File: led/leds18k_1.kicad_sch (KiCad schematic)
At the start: 32 parts, among them Q13 IPS70R1K4P7SAKMA1, Q2 IPS70R1K4P7SAKMA1, U1 LM397, U2 4N25, U5 4N25

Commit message: schematics with 5050 leds ready
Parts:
- removed D5: 1.5KE440A, Diode_THT:D_DO-15_P5.08mm_Vertical_KathodeUp, symbol Device:D_Zener
- removed D6, D7, D8, D9: 1N5408, Diode_THT:D_DO-41_SOD81_P10.16mm_Horizontal, symbol Diode:1N4007
- removed ESMR401VSN102MA50S_3: ESMR401VSN102MA50S, arduino-library:CAPPRD1000W180D3550H5250, symbol Device:C_Polarized
- removed L1: HCTI-220-5.8, arduino-library:HCTI22058, symbol Device:L
- removed LED1, LED10, LED11, LED12, LED13, LED14, LED2, LED3, LED4, LED5, LED6, LED7, LED8, LED9: L150-18705024000H0, arduino-library:L15065705024000H0, symbol L150-65705024000H0:L150-65705024000H0
- removed Q13, Q2: IPS70R1K4P7SAKMA1, arduino-library:TO229P240X654X875-3P, symbol IPS70R1K4P7SAKMA1:IPS70R1K4P7SAKMA1
- removed R1: RSF1JT1R00, arduino-library:RESAD2900W85L1100D450, symbol RSF1JT1R00:RSF1JT1R00
- removed R4, R5, R6: MFR-25FTE52-100K, Resistor_THT:R_Axial_DIN0204_L3.6mm_D1.6mm_P2.54mm_Vertical, symbol Device:R
- removed RH2: MFR50SFTE52-1K, Resistor_THT:R_Axial_DIN0204_L3.6mm_D1.6mm_P2.54mm_Vertical, symbol Device:R
- removed TH1: CL60, Resistor_THT:R_Axial_DIN0516_L15.5mm_D5.0mm_P7.62mm_Vertical, symbol Device:Thermistor_NTC
- removed U1: LM397, Package_TO_SOT_SMD:SOT-23-5, symbol Comparator:LM397
- removed U2, U5: 4N25, Package_DIP:DIP-6_W7.62mm, symbol Isolator:4N25
- added D31, D32, D33, D34: 1N5408, Diode_THT:D_DO-41_SOD81_P10.16mm_Horizontal, symbol Diode:1N4007
- added D35: 1.5KE440A, Diode_THT:D_DO-15_P5.08mm_Vertical_KathodeUp, symbol Device:D_Zener
- added ESMR401VSN102MA50S_7: ESMR401VSN102MA50S, arduino-library:CAPPRD1000W180D3550H5250, symbol Device:C_Polarized
- added L7: HCTI-220-5.8, arduino-library:HCTI22058, symbol Device:L
- added LED85, LED86, LED87, LED88, LED89, LED90, LED91, LED92, LED93, LED94, LED95, LED96, LED97, LED98: L150-18705024000H0, arduino-library:L15065705024000H0, symbol L150-65705024000H0:L150-65705024000H0
- added Q19, Q20: IPS70R1K4P7SAKMA1, arduino-library:TO229P240X654X875-3P, symbol IPS70R1K4P7SAKMA1:IPS70R1K4P7SAKMA1
- added R34: RSF1JT1R00, arduino-library:RESAD2900W85L1100D450, symbol RSF1JT1R00:RSF1JT1R00
- added R35, R36, R37: MFR-25FTE52-100K, Resistor_THT:R_Axial_DIN0204_L3.6mm_D1.6mm_P2.54mm_Vertical, symbol Device:R
- added RH7: MFR50SFTE52-1K, Resistor_THT:R_Axial_DIN0204_L3.6mm_D1.6mm_P2.54mm_Vertical, symbol Device:R
- added TH7: CL60, Resistor_THT:R_Axial_DIN0516_L15.5mm_D5.0mm_P7.62mm_Vertical, symbol Device:Thermistor_NTC
- added U20, U22: 4N25, Package_DIP:DIP-6_W7.62mm, symbol Isolator:4N25
- added U21: LM397, Package_TO_SOT_SMD:SOT-23-5, symbol Comparator:LM397
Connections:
- net CURRENT_DRIVER_PWM: now also RH7.2, U21.1 (-)
- net GND: now also D32.1 (K), D34.1 (K), ESMR401VSN102MA50S_7.2, R34.1, U20.2, U20.4, U21.2 (V-), U22.2, U22.4
- net LEDS_ON: now also U20.1
- net MAINS_LIVE: now also D33.1 (K), D34.2 (A)
- net MAINS_ZERO: now also D31.1 (K), D32.2 (A)
- net VDD: now also R36.1, R37.1, U20.6, U21.5 (V+)
- new net: LED85.1 (K_1), LED85.2 (A_1)
- new net: LED85.3 (K_2), LED86.4 (A_2)
- new net: LED85.4 (A_2), LED98.3 (K_2)
- new net: LED92.1 (K_1), LED92.2 (A_1)
- new net: LED92.3 (K_2), LED93.4 (A_2)
- new net: D35.1 (K), ESMR401VSN102MA50S_7.1, LED92.4 (A_2), TH7.2
- new net: Q19.3 (S), R34.2, U21.3 (+)
- new net: LED96.1 (K_1), LED96.2 (A_1)
- new net: LED96.3 (K_2), LED97.4 (A_2)
- new net: LED95.3 (K_2), LED96.4 (A_2)
- new net: R36.2, RH7.1, U21.4, U22.1
- new net: LED93.1 (K_1), LED93.2 (A_1)
- new net: LED93.3 (K_2), LED94.4 (A_2)
- new net: Q20.1 (G), R35.1, U22.5
- new net: L7.1, LED91.3 (K_2), Q20.2 (D), R35.2
- new net: Q19.2 (D), Q20.3 (S)
- new net: Q19.1 (G), U20.5
- new net: D31.2 (A), D33.2 (A), TH7.1
- new net: LED94.1 (K_1), LED94.2 (A_1)
- new net: LED94.3 (K_2), LED95.4 (A_2)
- new net: LED98.1 (K_1), LED98.2 (A_1)
- new net: LED97.3 (K_2), LED98.4 (A_2)
- new net: LED87.1 (K_1), LED87.2 (A_1)
- new net: LED87.3 (K_2), LED88.4 (A_2)
- new net: LED86.3 (K_2), LED87.4 (A_2)
- new net: LED88.1 (K_1), LED88.2 (A_1)
- new net: LED88.3 (K_2), LED89.4 (A_2)
- new net: LED86.1 (K_1), LED86.2 (A_1)
- new net: R37.2, U22.6
- new net: LED90.1 (K_1), LED90.2 (A_1)
- new net: LED90.3 (K_2), LED91.4 (A_2)
- new net: LED89.3 (K_2), LED90.4 (A_2)
- new net: LED89.1 (K_1), LED89.2 (A_1)
- new net: LED91.1 (K_1), LED91.2 (A_1)
- new net: D35.2 (A), L7.2
- new net: LED97.1 (K_1), LED97.2 (A_1)
- new net: LED95.1 (K_1), LED95.2 (A_1)

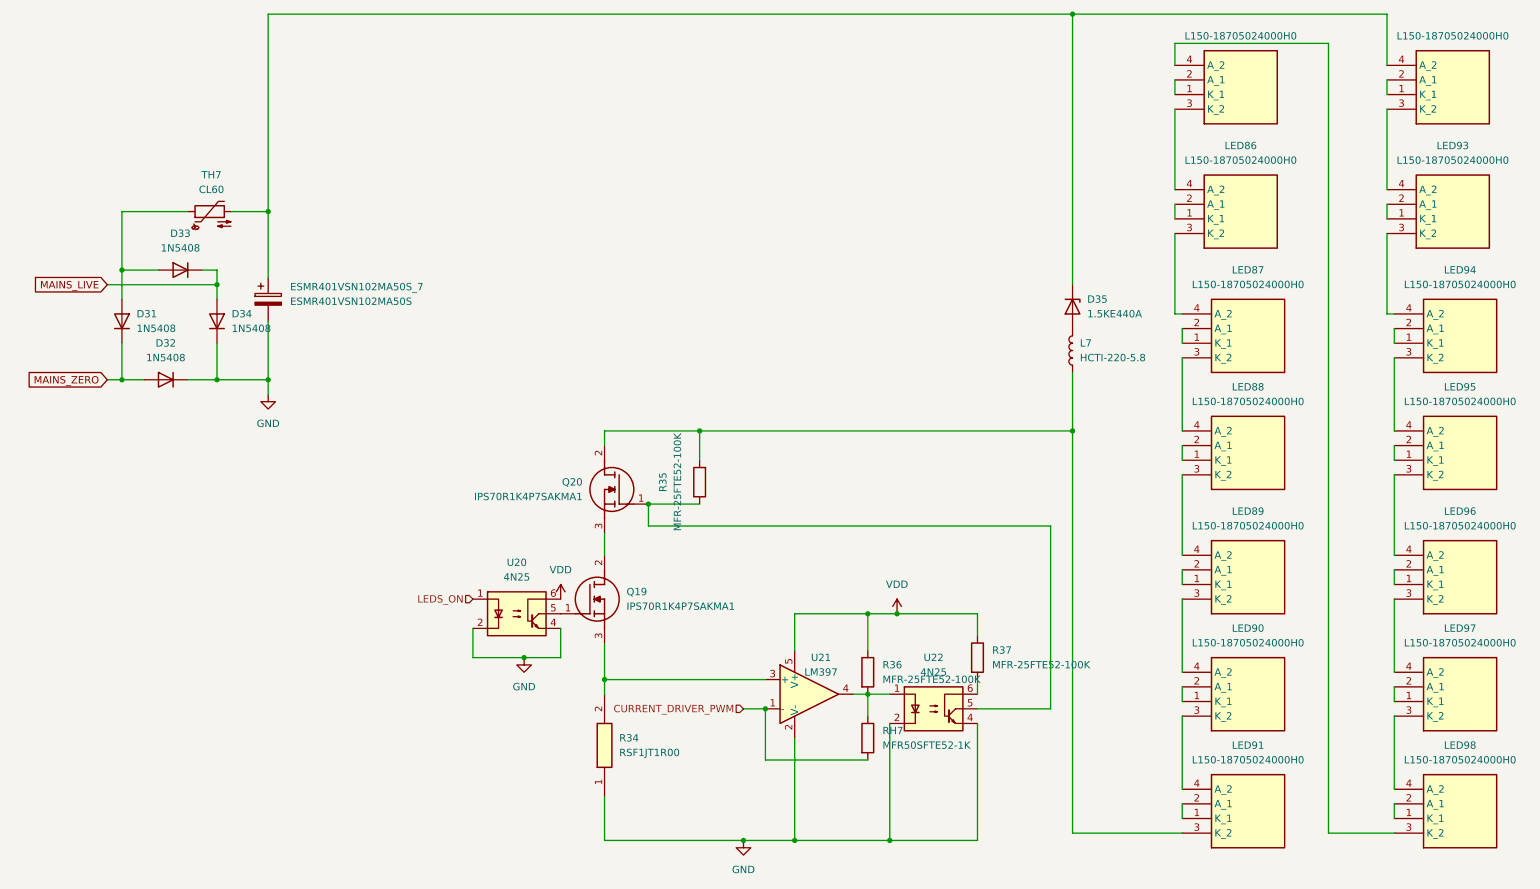
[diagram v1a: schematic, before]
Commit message: using single and dual top switch current driver circuits
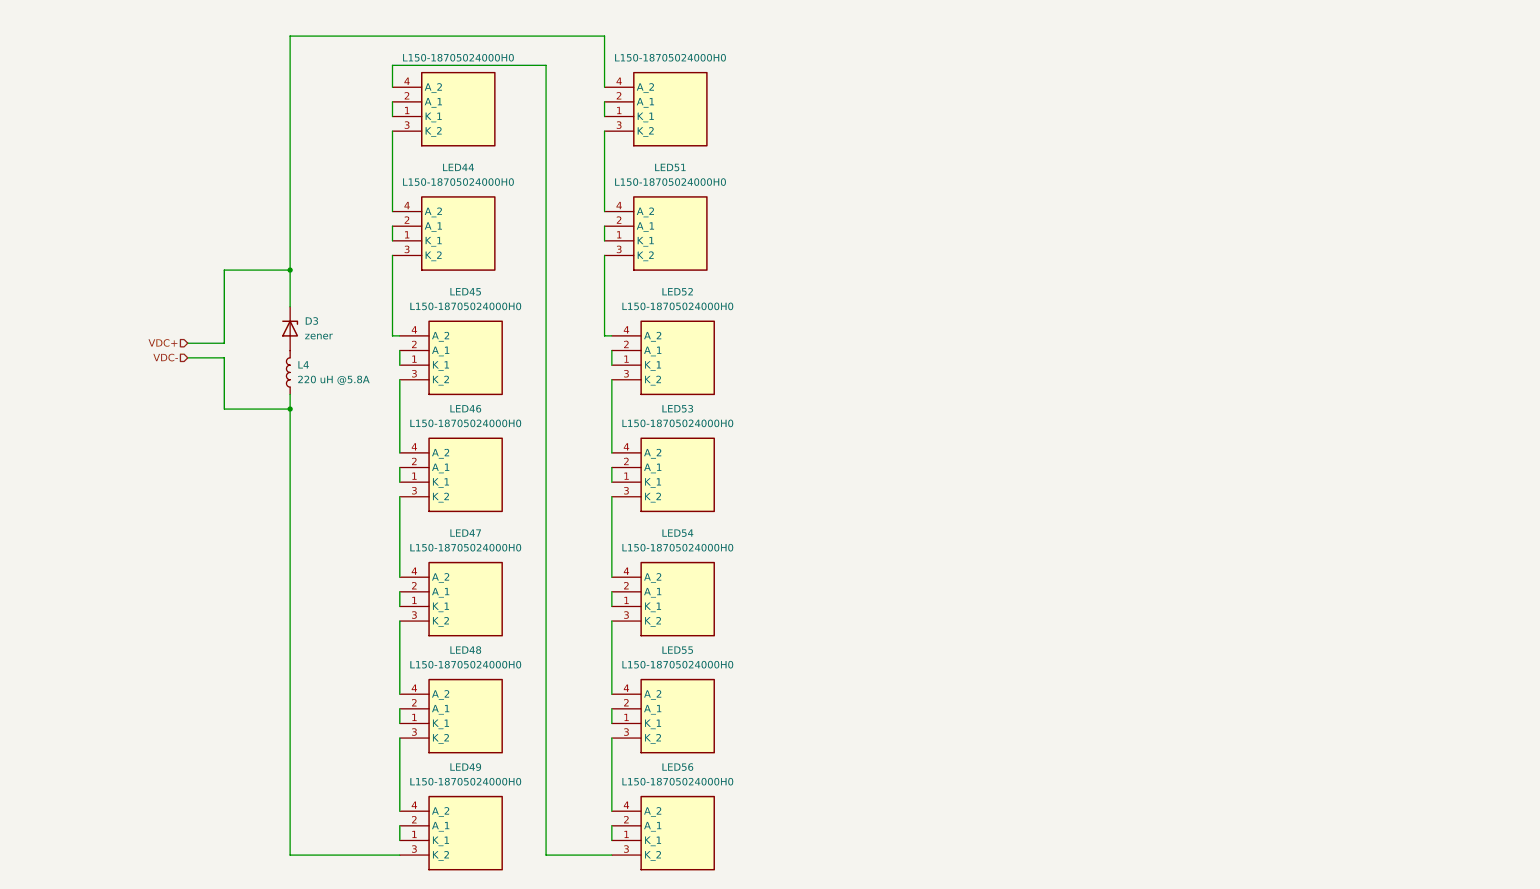
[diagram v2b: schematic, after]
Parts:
- removed D31, D32, D33, D34: 1N5408, Diode_THT:D_DO-41_SOD81_P10.16mm_Horizontal, symbol Diode:1N4007
- removed ESMR401VSN102MA50S_7: ESMR401VSN102MA50S, arduino-library:CAPPRD1000W180D3550H5250, symbol Device:C_Polarized
- removed Q19, Q20: IPS70R1K4P7SAKMA1, arduino-library:TO229P240X654X875-3P, symbol IPS70R1K4P7SAKMA1:IPS70R1K4P7SAKMA1
- removed R34: RSF1JT1R00, arduino-library:RESAD2900W85L1100D450, symbol RSF1JT1R00:RSF1JT1R00
- removed R35, R36, R37: MFR-25FTE52-100K, Resistor_THT:R_Axial_DIN0204_L3.6mm_D1.6mm_P2.54mm_Vertical, symbol Device:R
- removed RH7: MFR50SFTE52-1K, Resistor_THT:R_Axial_DIN0204_L3.6mm_D1.6mm_P2.54mm_Vertical, symbol Device:R
- removed TH7: CL60, Resistor_THT:R_Axial_DIN0516_L15.5mm_D5.0mm_P7.62mm_Vertical, symbol Device:Thermistor_NTC
- removed U20, U22: 4N25, Package_DIP:DIP-6_W7.62mm, symbol Isolator:4N25
- removed U21: LM397, Package_TO_SOT_SMD:SOT-23-5, symbol Comparator:LM397
- D3: renamed from D35; value 1.5KE440A -> zener; Mouser Part Number (none) -> 603-1.5KE440A/B
- L4: renamed from L7; value HCTI-220-5.8 -> 220 uH @5.8A; Mouser Part Number (none) -> 530-HCTI-220-5.8
- LED43: renamed from LED85; Mouser Part Number 997-L150657050240H0 -> 997-L15018705024000H
- LED44: renamed from LED86; Mouser Part Number 997-L150657050240H0 -> 997-L15018705024000H
- LED45: renamed from LED87; Mouser Part Number 997-L150657050240H0 -> 997-L15018705024000H
- LED46: renamed from LED88; Mouser Part Number 997-L150657050240H0 -> 997-L15018705024000H
- LED47: renamed from LED89; Mouser Part Number 997-L150657050240H0 -> 997-L15018705024000H
- LED48: renamed from LED90; Mouser Part Number 997-L150657050240H0 -> 997-L15018705024000H
- LED49: renamed from LED91; Mouser Part Number 997-L150657050240H0 -> 997-L15018705024000H
- LED50: renamed from LED92; Mouser Part Number 997-L150657050240H0 -> 997-L15018705024000H
- LED51: renamed from LED93; Mouser Part Number 997-L150657050240H0 -> 997-L15018705024000H
- LED52: renamed from LED94; Mouser Part Number 997-L150657050240H0 -> 997-L15018705024000H
- LED53: renamed from LED95; Mouser Part Number 997-L150657050240H0 -> 997-L15018705024000H
- LED54: renamed from LED96; Mouser Part Number 997-L150657050240H0 -> 997-L15018705024000H
- LED55: renamed from LED97; Mouser Part Number 997-L150657050240H0 -> 997-L15018705024000H
- LED56: renamed from LED98; Mouser Part Number 997-L150657050240H0 -> 997-L15018705024000H
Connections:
- net VDC+: now reaches D3.1 (K), LED50.4 (A_2)
- net VDC-: now reaches L4.1, LED49.3 (K_2)
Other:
- moved on the sheet: D3, L4, LED44, LED45, LED46, LED47, LED48, LED49, LED51, LED52, LED53, LED54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

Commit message: led pcb designed
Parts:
- added H12, H16: MountingHole_Pad, Connector_Pin:Pin_D1.0mm_L10.0mm_LooseFit, symbol Mechanical:MountingHole_Pad
- D3: footprint Diode_THT:D_DO-15_P5.08mm_Vertical_KathodeUp -> arduino-library:DIOM7959X262N; Mouser Part Number 603-1.5KE440A/B -> 833-SMCJ1.5KE440A-TP
- L4: footprint arduino-library:HCTI22058 -> arduino-library:Coil_6cmx1cm
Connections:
- net VDC+: now also H12.1
- net VDC-: now also H16.1
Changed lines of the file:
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@@
 	(paper "A4")
+	(junction
+		(at 54.61 73.66)
+		(diameter 0)
+		(color 0 0 0 0)
+	)
 	(junction
 		(at 69.85 85.09)
@@
 	)
 	(junction
+		(at 54.61 76.2)
+		(diameter 0)
+		(color 0 0 0 0)
+	)
+	(junction
 		(at 69.85 60.96)
 		(diameter 0)
@@
 	(wire
 		(pts
-			(xy 52.07 73.66) (xy 58.42 73.66)
+			(xy 52.07 73.66) (xy 54.61 73.66)
 		)
 		(stroke
@@
 	(wire
 		(pts
+			(xy 54.61 73.66) (xy 58.42 73.66)
+		)
+		(stroke
+			(width 0)
+			(type default)
+		)
+	)
+	(wire
+		(pts
 			(xy 69.85 20.32) (xy 69.85 60.96)
 		)
@@
 	(wire
 		(pts
-			(xy 52.07 76.2) (xy 58.42 76.2)
+			(xy 52.07 76.2) (xy 54.61 76.2)
 		)
 		(stroke
@@
 		(pts
 			(xy 88.9 121.92) (xy 88.9 134.62)
+		)
+		(stroke
+			(width 0)
+			(type default)
+		)
+	)
+	(wire
+		(pts
+			(xy 54.61 76.2) (xy 58.42 76.2)
 		)
 		(stroke
@@
 	)
 	(symbol
+		(lib_id "Mechanical:MountingHole_Pad")
+		(at 54.61 78.74 180)
+		(unit 1)
+		(exclude_from_sim no)
+		(in_bom no)
+		(on_board yes)
+		(dnp no)
+		(fields_autoplaced yes)
+		(property "Reference" "H16"
+			(at 57.15 78.7399 0)
+			(effects
+				(font
+					(size 1.27 1.27)
+				)
+				(justify right)
+			)
+		)
+		(property "Value" "MountingHole_Pad"
+			(at 57.15 81.2799 0)
+			(effects
+				(font
+					(size 1.27 1.27)
+				)
+				(justify right)
+			)
+		)
+		(property "Footprint" "Connector_Pin:Pin_D1.0mm_L10.0mm_LooseFit"
+			(at 54.61 78.74 0)
+			(effects
+				(font
+					(size 1.27 1.27)
+				)
+				(hide yes)
+			)
+		)
+		(property "Datasheet" "~"
+			(at 54.61 78.74 0)
+			(effects
+				(font
+					(size 1.27 1.27)
+				)
+				(hide yes)
+			)
+		)
+		(property "Description" "Mounting Hole with connection"
+			(at 54.61 78.74 0)
+			(effects
+				(font
+					(size 1.27 1.27)
+				)
+				(hide yes)
+			)
+		)
+		(pin "1"
+		)
+		(instances
+			(project "led"
+				(path "/3f432d6c-3758-4345-b186-9310705dc61b/4657a6da-42a0-4c37-9dff-046ab29fe1ba"
+					(reference "H16")
+					(unit 1)
+				)
+				(path "/3f432d6c-3758-4345-b186-9310705dc61b/5aec1ce1-45e4-46e9-8146-4644b64be076"
+					(reference "H17")
+					(unit 1)
+				)
+				(path "/3f432d6c-3758-4345-b186-9310705dc61b/a148affd-8e36-468c-8c01-ab2086054996"
+					(reference "H18")
+					(unit 1)
+				)
+				(path "/3f432d6c-3758-4345-b186-9310705dc61b/e5c4d2d5-aef7-4d79-b2d9-7e80d0bdca31"
+					(reference "H19")
+					(unit 1)
+				)
+			)
+		)
+	)
+	(symbol
 		(lib_id "L150-65705024000H0:L150-65705024000H0")
 		(at 88.9 80.01 0)
@@
 			)
 		)
-		(property "Footprint" "arduino-library:HCTI22058"
+		(property "Footprint" "arduino-library:Coil_6cmx1cm"
 			(at 69.85 78.74 0)
 			(effects
@@
 			)
 		)
-		(property "Description" "Inductor"
+		(property "Description" "Inductor coil radius=1cm, length=5.5cm, turns=3*55=165, wire radius=1mm air or wood core"
 			(at 69.85 78.74 0)
 			(effects
@@
 			)
 		)
-		(property "Footprint" "Diode_THT:D_DO-15_P5.08mm_Vertical_KathodeUp"
+		(property "Footprint" "arduino-library:DIOM7959X262N"
 			(at 69.85 71.12 0)
 			(effects
@@
 			)
 		)
-		(property "Datasheet" "https://www.littelfuse.com/assetdocs/tvs-diodes-1-5ke-datasheet?assetguid=9D02C7D2-86A5-4BFF-9251-966D6AF02BF7"
+		(property "Datasheet" "https://hu.mouser.com/datasheet/3/225/1/SMCJ1.5KE6.8(C)A-SMCJ1.5KE550(C)A(DO-214AB).pdf"
 			(at 69.85 71.12 0)
 			(effects
@@
 			)
 		)
-		(property "Mouser Part Number" "603-1.5KE440A/B"
+		(property "Mouser Part Number" "833-SMCJ1.5KE440A-TP"
 			(at 69.85 71.12 90)
 			(effects
@@
 					(unit 1)
 				)
+			)
+		)
+	)
+	(symbol
+		(lib_id "Mechanical:MountingHole_Pad")
+		(at 54.61 71.12 0)
+		(unit 1)
+		(exclude_from_sim no)
+		(in_bom no)
+		(on_board yes)
+		(dnp no)
+		(fields_autoplaced yes)
+		(property "Reference" "H12"
+			(at 57.15 68.5799 0)
+			(effects
+				(font
+					(size 1.27 1.27)
+				)
+				(justify left)
+			)
+		)
+		(property "Value" "MountingHole_Pad"
+			(at 57.15 71.1199 0)
+			(effects
+				(font
+					(size 1.27 1.27)
+				)
+				(justify left)
+			)
+		)
+		(property "Footprint" "Connector_Pin:Pin_D1.0mm_L10.0mm_LooseFit"
+			(at 54.61 71.12 0)
+			(effects
+				(font
+					(size 1.27 1.27)
+				)
+				(hide yes)
+			)
+		)
+		(property "Datasheet" "~"
+			(at 54.61 71.12 0)
+			(effects
+				(font
+					(size 1.27 1.27)
+				)
+				(hide yes)
+			)
+		)
+		(property "Description" "Mounting Hole with connection"
+			(at 54.61 71.12 0)
+			(effects
+				(font
+					(size 1.27 1.27)
+				)
+				(hide yes)
+			)
+		)
+		(pin "1"
+		)
+		(instances
+			(project "led"
+				(path "/3f432d6c-3758-4345-b186-9310705dc61b/4657a6da-42a0-4c37-9dff-046ab29fe1ba"
+					(reference "H12")
+					(unit 1)
+				)
+				(path "/3f432d6c-3758-4345-b186-9310705dc61b/5aec1ce1-45e4-46e9-8146-4644b64be076"
+					(reference "H13")
+					(unit 1)
+				)
+				(path "/3f432d6c-3758-4345-b186-9310705dc61b/a148affd-8e36-468c-8c01-ab2086054996"
+					(reference "H14")
+					(unit 1)
+				)
+				(path "/3f432d6c-3758-4345-b186-9310705dc61b/e5c4d2d5-aef7-4d79-b2d9-7e80d0bdca31"
+					(reference "H15")
+					(unit 1)
+				)
